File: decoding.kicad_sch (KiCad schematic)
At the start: 30 parts

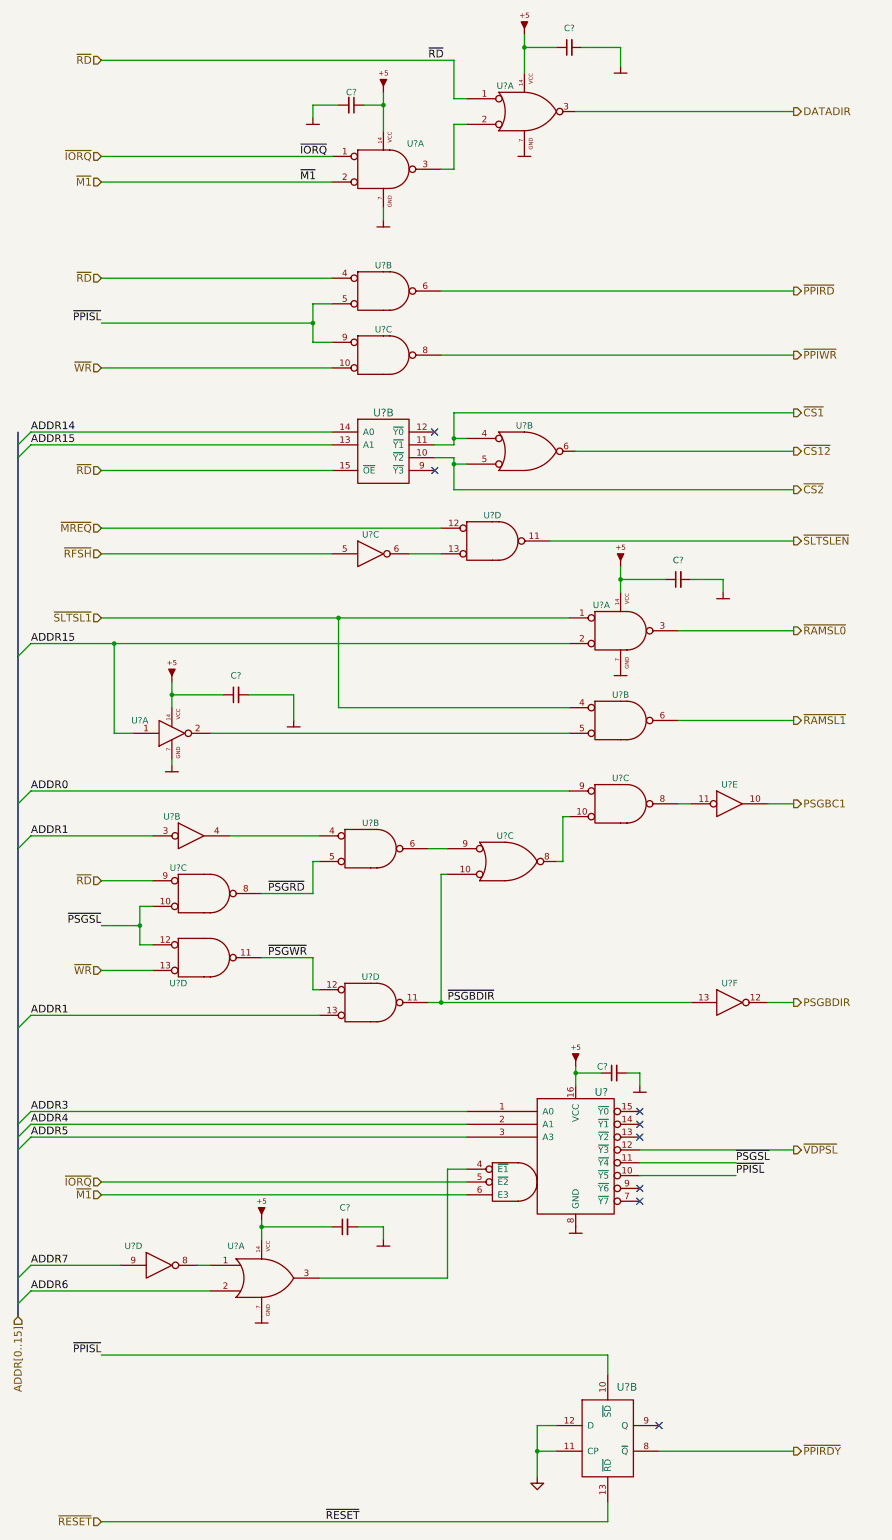
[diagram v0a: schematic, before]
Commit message: Implement power transform circuit
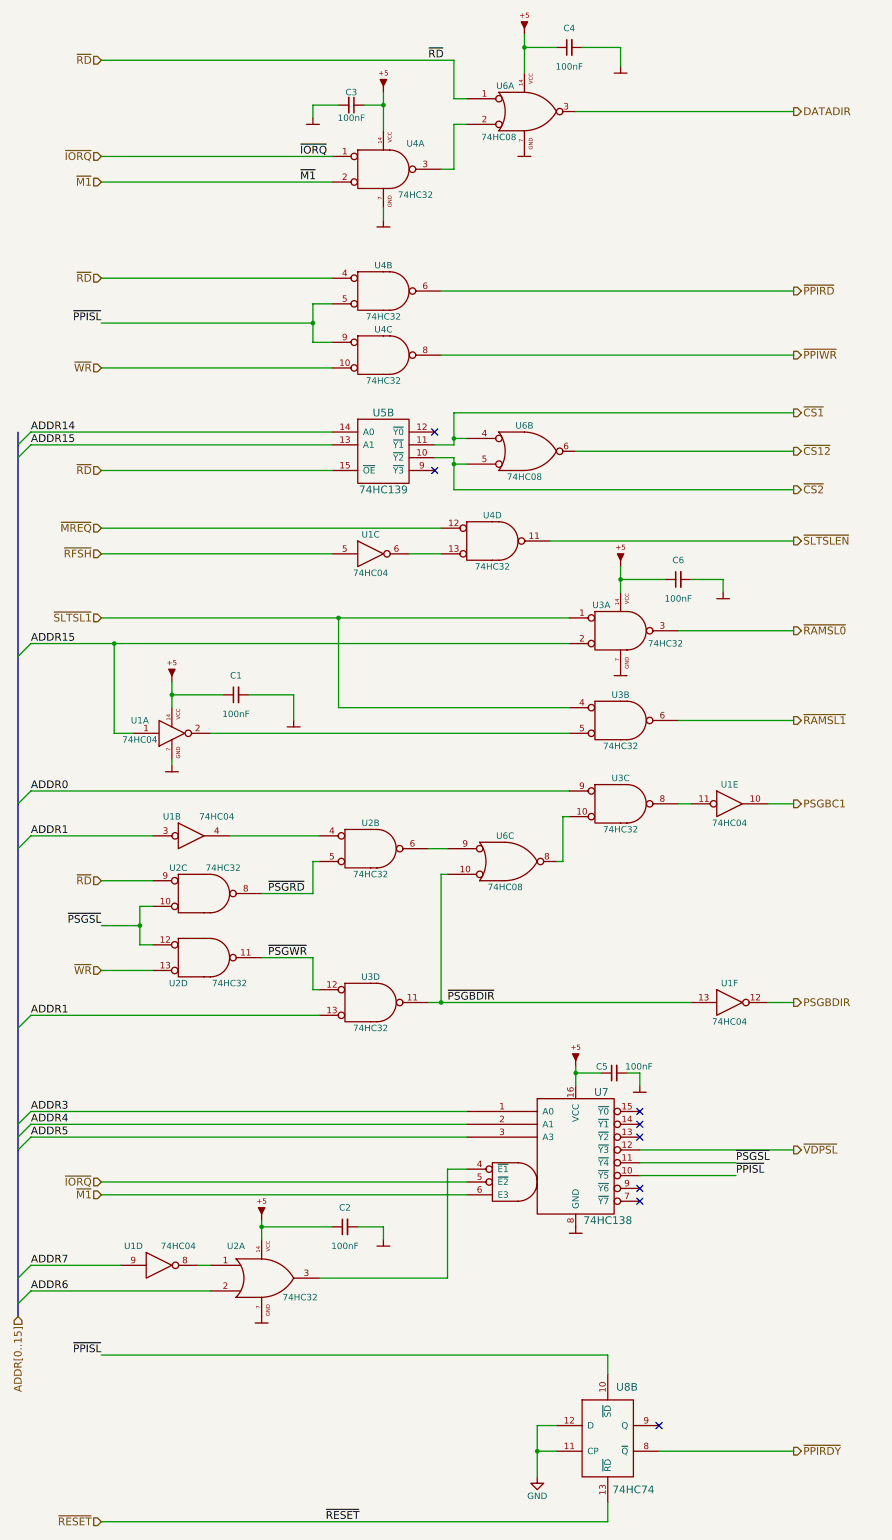
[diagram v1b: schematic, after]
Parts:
- C1, C2, C3, C4, C5, C6: renamed from C?; value (none) -> 100nF; footprint (none) -> artemisa:Disc_capacitor
- U1: renamed from U?; value (none) -> 74HC04; footprint (none) -> artemisa:DIP-14_300
- U2, U3, U4: renamed from U?; value (none) -> 74HC32; footprint (none) -> artemisa:DIP-14_300
- U5: renamed from U?; value (none) -> 74HC139; footprint (none) -> artemisa:DIP-16_300
- U6: renamed from U?; value (none) -> 74HC08; footprint (none) -> artemisa:DIP-14_300
- U7: renamed from U?; value (none) -> 74HC138; footprint (none) -> artemisa:DIP-16_300
- U8: renamed from U?; value (none) -> 74HC74; footprint (none) -> artemisa:DIP-14_300
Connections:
- net VCC: now also C1.1, C2.1, C3.1, C4.1, C5.1, C6.1, U1.14 (VCC), U2.14 (VCC), U3.14 (VCC), U4.14 (VCC), U6.14 (VCC), U7.16 (VCC)
